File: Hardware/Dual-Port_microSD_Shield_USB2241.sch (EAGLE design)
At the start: 84 parts, among them IC1 USB224X_2241, J2 MICRO-SD-PUSH-PUSH-EXT-PIN, J3 AVR_SPI_PROG_3X2TESTPOINTS, J4 THING_PLUS, Q1 20V/4.2A/52mΩ/1.4W, Q2 20V/0.2A/8MHz/1.2Ω/1Vth, Q3 20V/4.2A/52mΩ/1.4W, Q4 20V/4.2A/52mΩ/1.4W, Q6 20V/4.2A/52mΩ/1.4W, U1 3.3V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

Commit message: Add silk. Replace xtal caps with calculated values. Finishing touches...
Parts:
- C12, C17: value 15pF -> 12pF; device SparkFun-Capacitors:15PF-0402T-50V-5% -> SparkFun-Capacitors:12PF-0402T-50V-5%
- LOGO5: value SFE_LOGO_NAME_FLAME.2_INCH -> SFE_LOGO_NAME_FLAME.1_INCH; device SparkFun-Aesthetics:SFE_LOGO_NAME_FLAME.2_INCH -> SparkFun-Aesthetics:SFE_LOGO_NAME_FLAME.1_INCH
- R4: value 4.7k -> 10k; device SparkFun-Resistors:4.7KOHM-0402T-1/16W-1% -> SparkFun-Resistors:10KOHM-0402T-1/16W-1%
- renumbered RX to TXD, TX to RXD
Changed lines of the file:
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@@
 <part name="J3" library="SparkFun-Connectors" deviceset="AVR_SPI_PROG_3X2" device="TESTPOINTS"/>
 <part name="GND11" library="SparkFun-PowerSymbols" deviceset="GND" device=""/>
-<part name="R4" library="SparkFun-Resistors" deviceset="4.7KOHM" device="-0402T-1/16W-1%" value="4.7k"/>
+<part name="R4" library="SparkFun-Resistors" deviceset="10KOHM" device="-0402T-1/16W-1%" value="10k"/>
 <part name="R2" library="SparkFun-Resistors" deviceset="10KOHM" device="-0402T-1/16W-1%" value="10k"/>
 <part name="R3" library="SparkFun-Resistors" deviceset="10KOHM" device="-0402T-1/16W-1%" value="10k"/>
@@
 <part name="Y1" library="SparkFun-Clocks" deviceset="CRYSTAL-24MHZ" device="-SMD-2.0X1.6MM" value="24MHz"/>
 <part name="R12" library="SparkFun-Resistors" deviceset="1MOHM" device="-0402T-1/16W-5%" value="1M"/>
-<part name="C12" library="SparkFun-Capacitors" deviceset="15PF" device="-0402T-50V-5%" value="15pF"/>
-<part name="C17" library="SparkFun-Capacitors" deviceset="15PF" device="-0402T-50V-5%" value="15pF"/>
+<part name="C12" library="SparkFun-Capacitors" deviceset="12PF" device="-0402T-50V-5%" value="12pF"/>
+<part name="C17" library="SparkFun-Capacitors" deviceset="12PF" device="-0402T-50V-5%" value="12pF"/>
 <part name="GND26" library="SparkFun-PowerSymbols" deviceset="GND" device=""/>
 <part name="GND32" library="SparkFun-PowerSymbols" deviceset="GND" device=""/>
@@
 <part name="GND" library="SparkFun-Connectors" deviceset="TEST-POINT" device="3"/>
 <part name="SD_WP" library="SparkFun-Connectors" deviceset="TEST-POINT" device="3"/>
-<part name="TX" library="SparkFun-Jumpers" deviceset="JUMPER-SMT_2_NO" device="_SILK" package3d_urn="urn:adsk.eagle:package:39279/1"/>
-<part name="RX" library="SparkFun-Jumpers" deviceset="JUMPER-SMT_2_NO" device="_SILK" package3d_urn="urn:adsk.eagle:package:39279/1"/>
+<part name="RXD" library="SparkFun-Jumpers" deviceset="JUMPER-SMT_2_NO" device="_SILK" package3d_urn="urn:adsk.eagle:package:39279/1"/>
+<part name="TXD" library="SparkFun-Jumpers" deviceset="JUMPER-SMT_2_NO" device="_SILK" package3d_urn="urn:adsk.eagle:package:39279/1"/>
 <part name="C18" library="SparkFun-Capacitors" deviceset="2.2UF" device="-0402_TIGHT-10V-10%-X5R" value="2.2uF"/>
 <part name="GND33" library="SparkFun-PowerSymbols" deviceset="GND" device=""/>
@@
 <part name="SUPPLY32" library="SparkFun-PowerSymbols" deviceset="3.3V" device=""/>
 <part name="LOGO4" library="SparkFun-Aesthetics" deviceset="SFE_LOGO_FLAME" device=".2_INCH"/>
-<part name="LOGO5" library="SparkFun-Aesthetics" deviceset="SFE_LOGO_NAME_FLAME" device=".2_INCH"/>
+<part name="LOGO5" library="SparkFun-Aesthetics" deviceset="SFE_LOGO_NAME_FLAME" device=".1_INCH" value="SFE_LOGO_NAME_FLAME.1_INCH"/>
 <part name="SDIO_!RESET!" library="SparkFun-Connectors" deviceset="TEST-POINT" device="3"/>
 </parts>
@@
 <attribute name="NAME" x="271.78" y="193.04" size="1.778" layer="95" font="vector"/>
 </instance>
-<instance part="TX" gate="G$1" x="68.58" y="48.26" smashed="yes">
+<instance part="RXD" gate="G$1" x="68.58" y="48.26" smashed="yes">
 <attribute name="NAME" x="72.39" y="49.784" size="1.778" layer="95" font="vector" align="center"/>
 </instance>
-<instance part="RX" gate="G$1" x="68.58" y="45.72" smashed="yes">
+<instance part="TXD" gate="G$1" x="68.58" y="45.72" smashed="yes">
 <attribute name="NAME" x="72.39" y="47.244" size="1.778" layer="95" font="vector" align="center"/>
 </instance>
@@
 </segment>
 <segment>
-<pinref part="TX" gate="G$1" pin="2"/>
+<pinref part="RXD" gate="G$1" pin="2"/>
 <wire x1="73.66" y1="48.26" x2="76.2" y2="48.26" width="0.1524" layer="91"/>
 <label x="76.2" y="48.26" size="1.27" layer="95" font="vector" xref="yes"/>
@@
 </segment>
 <segment>
-<pinref part="RX" gate="G$1" pin="2"/>
+<pinref part="TXD" gate="G$1" pin="2"/>
 <wire x1="73.66" y1="45.72" x2="76.2" y2="45.72" width="0.1524" layer="91"/>
 <label x="76.2" y="45.72" size="1.27" layer="95" font="vector" xref="yes"/>
@@
 <segment>
 <pinref part="J4" gate="G$1" pin="TX"/>
-<pinref part="TX" gate="G$1" pin="1"/>
+<pinref part="RXD" gate="G$1" pin="1"/>
 <wire x1="55.88" y1="48.26" x2="63.5" y2="48.26" width="0.1524" layer="91"/>
 </segment>
@@
 <segment>
 <pinref part="J4" gate="G$1" pin="RX"/>
-<pinref part="RX" gate="G$1" pin="1"/>
+<pinref part="TXD" gate="G$1" pin="1"/>
 <wire x1="55.88" y1="45.72" x2="63.5" y2="45.72" width="0.1524" layer="91"/>
 </segment>

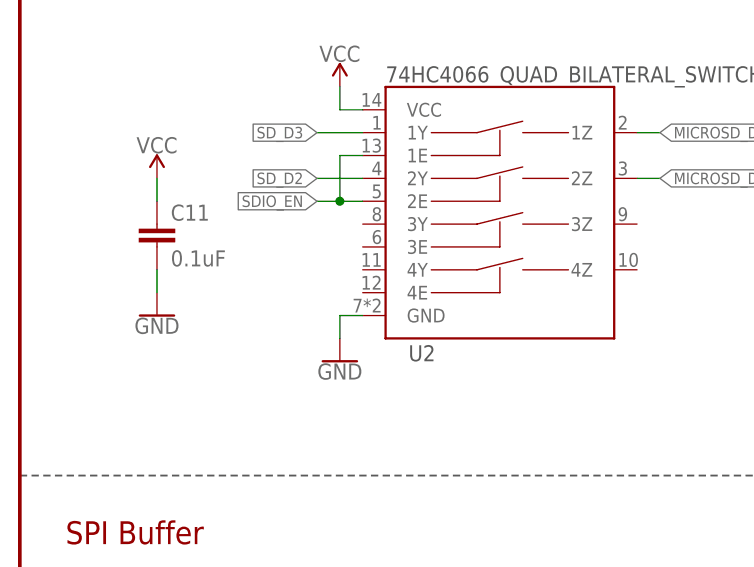
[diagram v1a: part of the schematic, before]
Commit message: Corrected 74HC4066 footprint. Swapped U4 and U5.
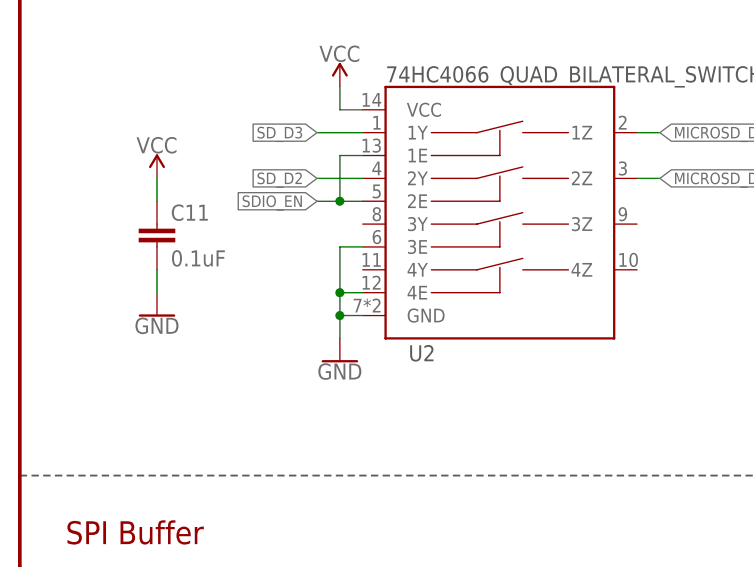
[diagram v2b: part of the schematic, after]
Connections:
- net N$20 renamed GPIO4
- net N$21 renamed GPIO7
- net N$24 renamed SD_WP
- net N$6 renamed SDIO_!RESET!
- net N$8 renamed GPIO2
- net GND: now also U2.3E, U2.4E
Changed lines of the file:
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@@
 <setting verticaltext="up"/>
 </settings>
-<grid distance="0.1" unitdist="inch" unit="inch" style="lines" multiple="1" display="no" altdistance="0.05" altunitdist="inch" altunit="inch"/>
+<grid distance="0.05" unitdist="inch" unit="inch" style="lines" multiple="1" display="yes" altdistance="0.005" altunitdist="inch" altunit="inch"/>
 <layers>
 <layer number="1" name="Top" color="4" fill="1" visible="no" active="no"/>
@@
 <pinref part="GND1" gate="1" pin="GND"/>
 <wire x1="35.56" y1="193.04" x2="35.56" y2="190.5" width="0.1524" layer="91"/>
+<pinref part="U2" gate="G$1" pin="3E"/>
+<wire x1="38.1" y1="200.66" x2="35.56" y2="200.66" width="0.1524" layer="91"/>
+<wire x1="35.56" y1="200.66" x2="35.56" y2="195.58" width="0.1524" layer="91"/>
+<junction x="35.56" y="193.04"/>
+<pinref part="U2" gate="G$1" pin="4E"/>
+<wire x1="35.56" y1="195.58" x2="35.56" y2="193.04" width="0.1524" layer="91"/>
+<wire x1="38.1" y1="195.58" x2="35.56" y2="195.58" width="0.1524" layer="91"/>
+<junction x="35.56" y="195.58"/>
 </segment>
 <segment>
@@
 </segment>
 </net>
-<net name="N$6" class="0">
+<net name="SDIO_!RESET!" class="0">
 <segment>
 <pinref part="IC1" gate="G$1" pin="!RESET!"/>
@@
 </segment>
 </net>
-<net name="N$8" class="0">
+<net name="GPIO2" class="0">
 <segment>
 <pinref part="IC1" gate="G$1" pin="GPIO2"/>
@@
 </segment>
 </net>
-<net name="N$20" class="0">
+<net name="GPIO4" class="0">
 <segment>
 <pinref part="IC1" gate="G$1" pin="GPIO4"/>
@@
 </segment>
 </net>
-<net name="N$21" class="0">
+<net name="GPIO7" class="0">
 <segment>
 <pinref part="IC1" gate="G$1" pin="GPIO7"/>
@@
 </segment>
 </net>
-<net name="N$24" class="0">
+<net name="SD_WP" class="0">
 <segment>
 <pinref part="SD_WP" gate="G$1" pin="1"/>

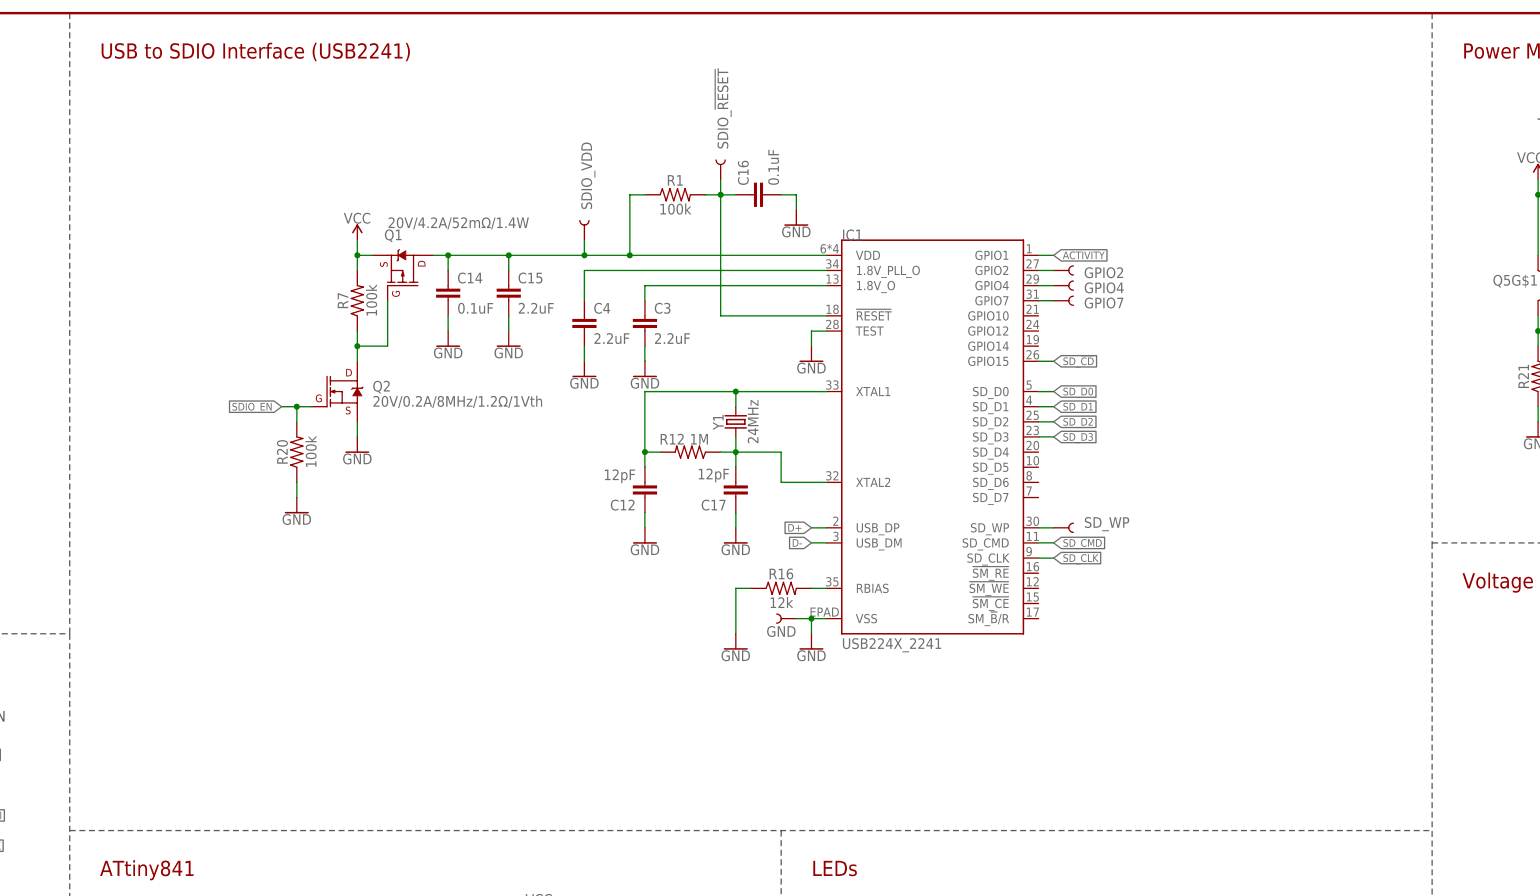
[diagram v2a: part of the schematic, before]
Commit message: Add footprint for optional I2C EEPROM
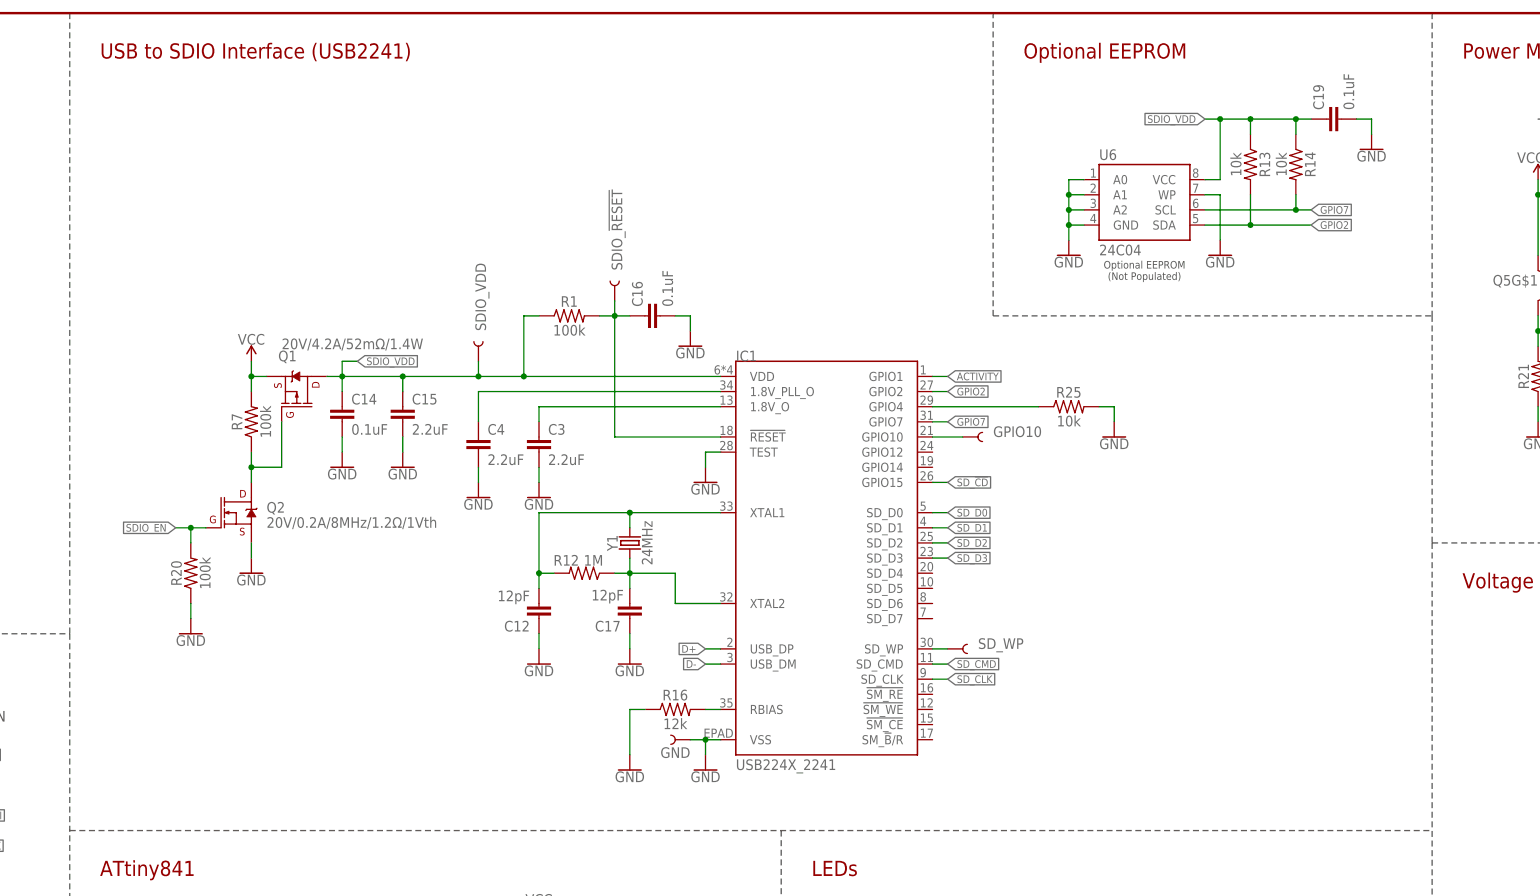
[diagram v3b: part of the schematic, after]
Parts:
- removed GPIO2, GPIO4, GPIO7: TEST-POINT3, SparkFun-Connectors:TEST-POINT3
- added C19: 0.1uF, SparkFun-Capacitors:0.1UF-0402T-6.3V-10%-X7R
- added GPIO10: TEST-POINT3, SparkFun-Connectors:TEST-POINT3
- added R13, R14, R25: 10k, SparkFun-Resistors:10KOHM-0402T-1/16W-1%
- added U6: 24C04, SparkFun-IC-Memory:EEPROM-I2C256K
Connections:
- new net GPIO10: GPIO10.1, IC1.GPIO10
- net GND: now also C19.2, R25.2, U6.A0, U6.A1, U6.A2, U6.GND, U6.WP
- net GPIO2: now also R13.2, U6.SDA; no longer GPIO2.1
- net GPIO4: now also R25.1; no longer GPIO4.1
- net GPIO7: now also R14.2, U6.SCL; no longer GPIO7.1
- net SDIO_VDD: now also C19.1, R13.1, R14.1, U6.VCC
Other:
- note added: "Optional EEPROM"
- note added: "Optional EEPROM (Not Populated)"
- moved on the sheet: C12, C14, C15, C16, C17, C3, C4, GND, IC1, Q1, Q2, R1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
